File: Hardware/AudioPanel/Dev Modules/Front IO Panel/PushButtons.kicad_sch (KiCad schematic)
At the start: 38 parts, among them CN3 4x 10nF, CN4 4x 10nF, CN5 4x 10nF, U10 74HC14, U11 74HC14, U16 MCP23017_ML

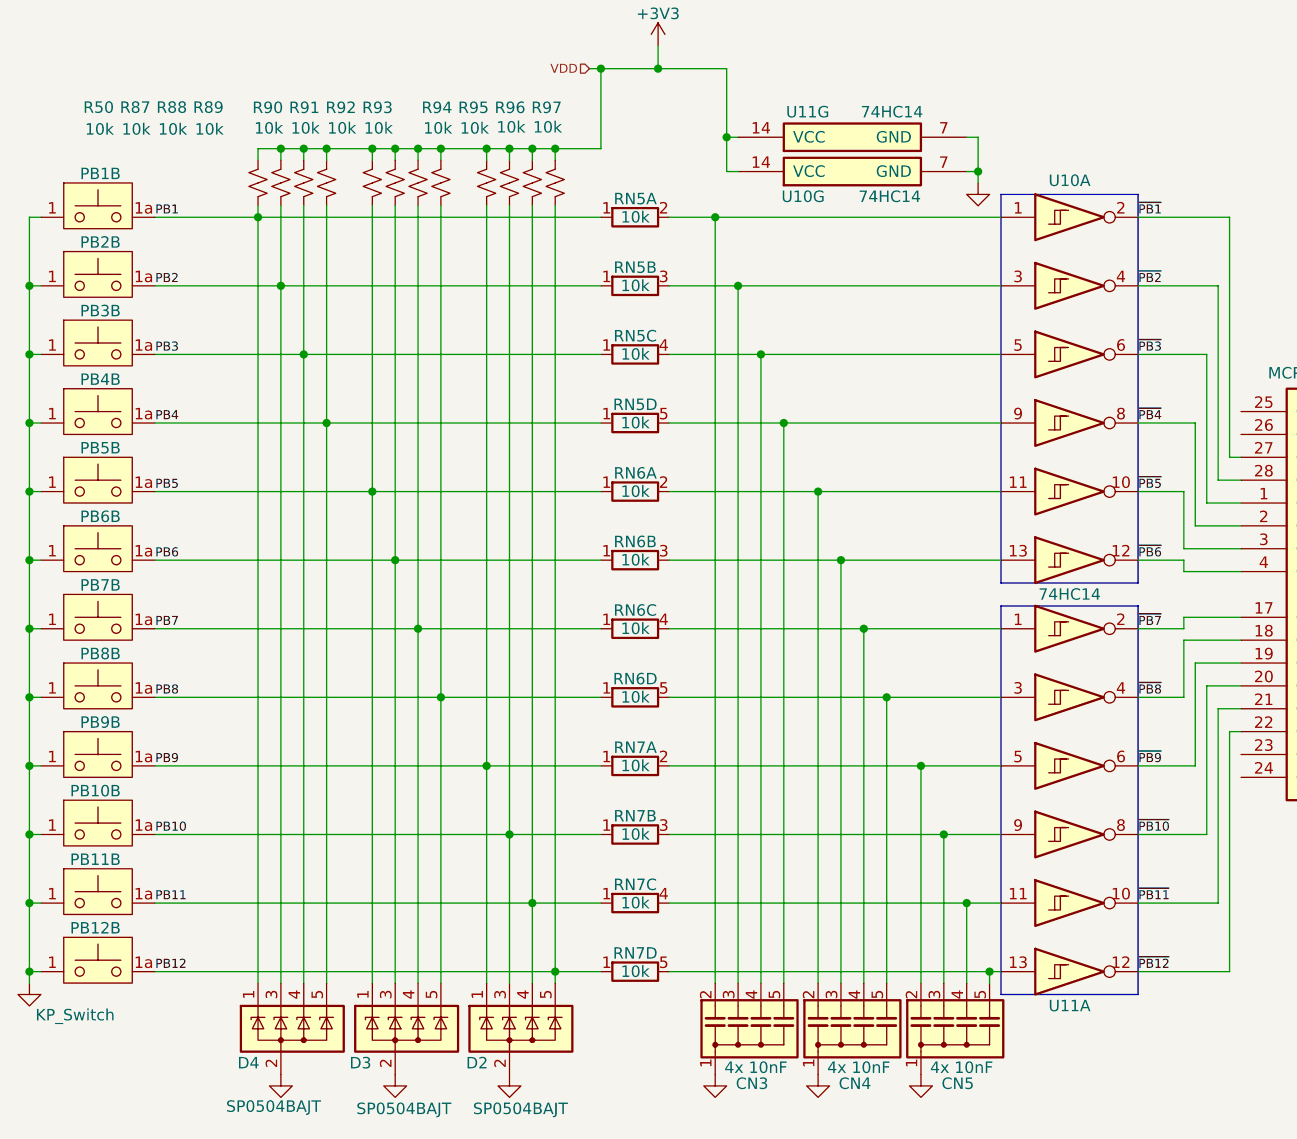
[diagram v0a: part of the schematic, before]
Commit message: Adding LEDs
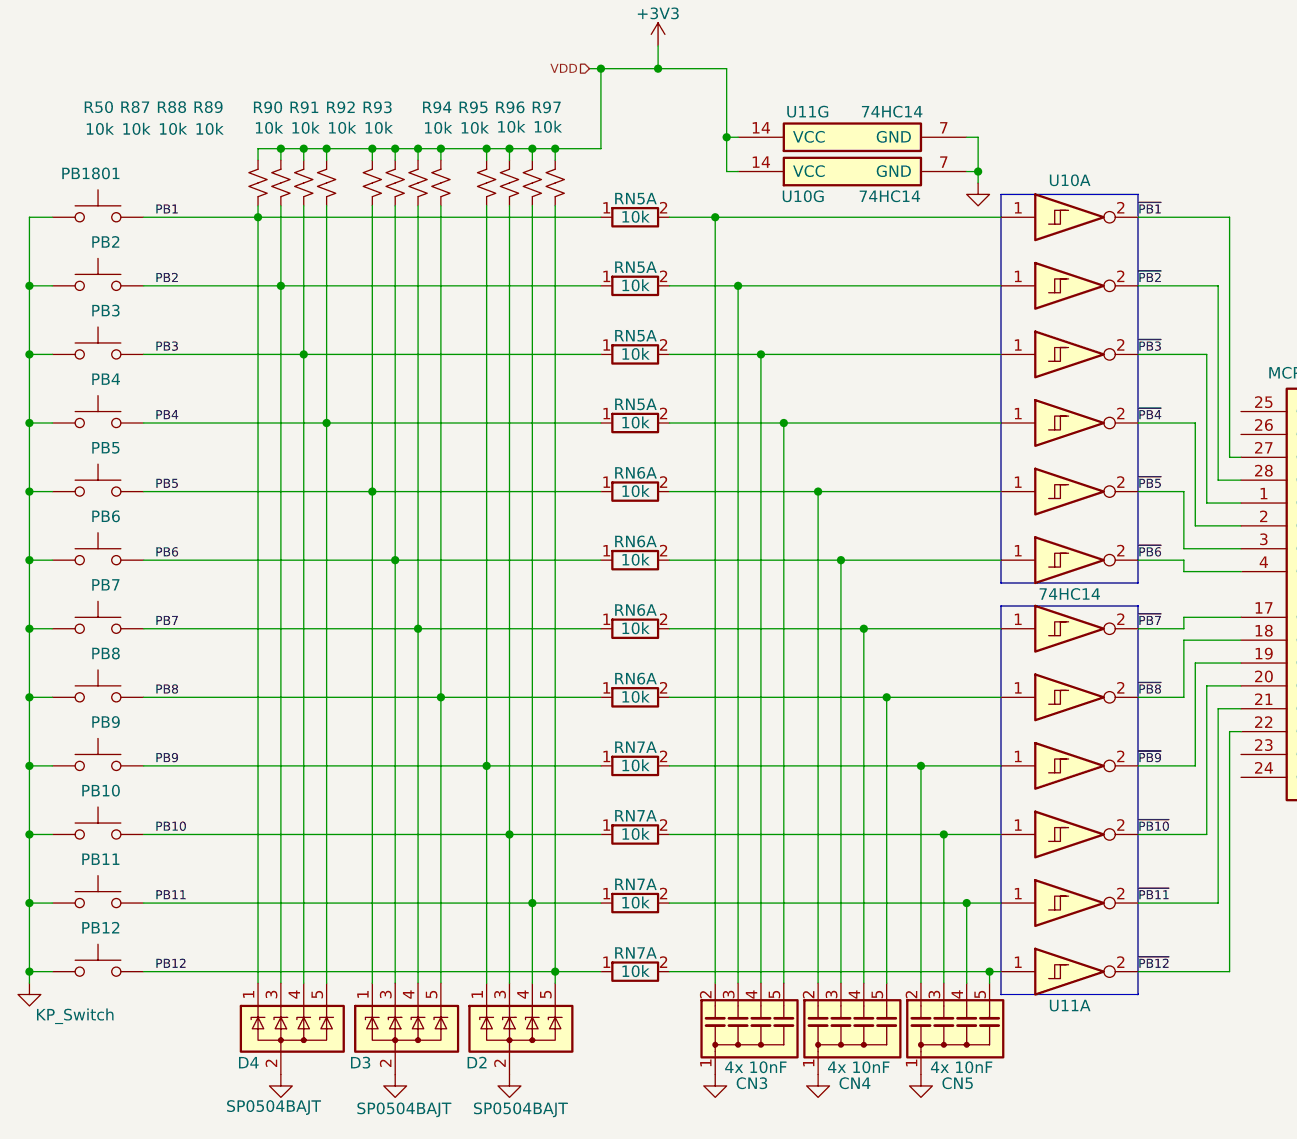
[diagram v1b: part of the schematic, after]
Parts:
- removed PB1: KP_Switch, symbol AudioPanelLibrary:KP_Switch
- added PB1801: KP_Switch, symbol Switch:SW_Push
- PB10, PB11, PB12, PB2, PB3, PB4, PB5, PB6, PB7, PB8, PB9: symbol AudioPanelLibrary:KP_Switch -> Switch:SW_Push
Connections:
- net GND: now also PB1801.1
- net PB1: now also PB1801.2
- net PB10: now also PB10.2; no longer PB10.1a (A)
- net PB11: now also PB11.2; no longer PB11.1a (A)
- net PB12: now also PB12.2; no longer PB12.1a (A)
- net PB2: now also PB2.2; no longer PB2.1a (A)
- net PB3: now also PB3.2; no longer PB3.1a (A)
- net PB4: now also PB4.2; no longer PB4.1a (A)
- net PB5: now also PB5.2; no longer PB5.1a (A)
- net PB6: now also PB6.2; no longer PB6.1a (A)
- net PB7: now also PB7.2; no longer PB7.1a (A)
- net PB8: now also PB8.2; no longer PB8.1a (A)
- net PB9: now also PB9.2; no longer PB9.1a (A)
- net ~{PB10}: now also U11.2; no longer U11.8
- net ~{PB11}: now also U11.2; no longer U11.10
- net ~{PB12}: now also U11.2; no longer U11.12
- net ~{PB2}: now also U10.2; no longer U10.4
- net ~{PB3}: now also U10.2; no longer U10.6
- net ~{PB4}: now also U10.2; no longer U10.8
- net ~{PB5}: now also U10.2; no longer U10.10
- net ~{PB6}: now also U10.2; no longer U10.12
- net ~{PB8}: now also U11.2; no longer U11.4
- net ~{PB9}: now also U11.2; no longer U11.6
- net at CN4.2 (C1), RN6.2 (R1.2): now also U10.1; no longer U10.11
- net at CN5.2 (C1), RN7.2 (R1.2): now also U11.1; no longer U11.5
- net at CN4.4 (C3), U11.1: now also RN6.2 (R1.2); no longer RN6.4 (R3.2)
- new net: CN5.3 (C2), RN7.2 (R1.2), U11.1
- new net: CN5.4 (C3), RN7.2 (R1.2), U11.1
- new net: CN5.5 (C4), RN7.2 (R1.2), U11.1
- new net: CN3.5 (C4), RN5.2 (R1.2), U10.1
- new net: CN3.4 (C3), RN5.2 (R1.2), U10.1
- new net: CN4.5 (C4), RN6.2 (R1.2), U11.1
- new net: CN3.3 (C2), RN5.2 (R1.2), U10.1
- new net: CN4.3 (C2), RN6.2 (R1.2), U10.1

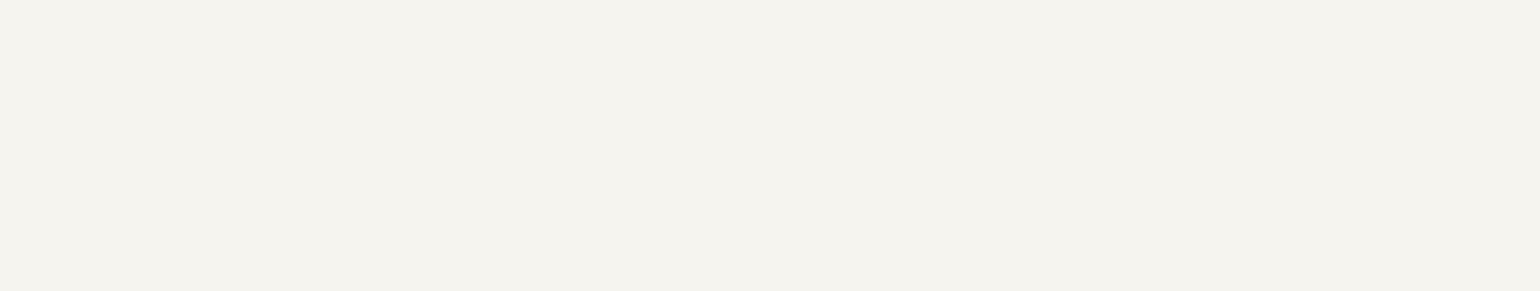
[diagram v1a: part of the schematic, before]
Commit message: Moved LEDs to pushbutton page
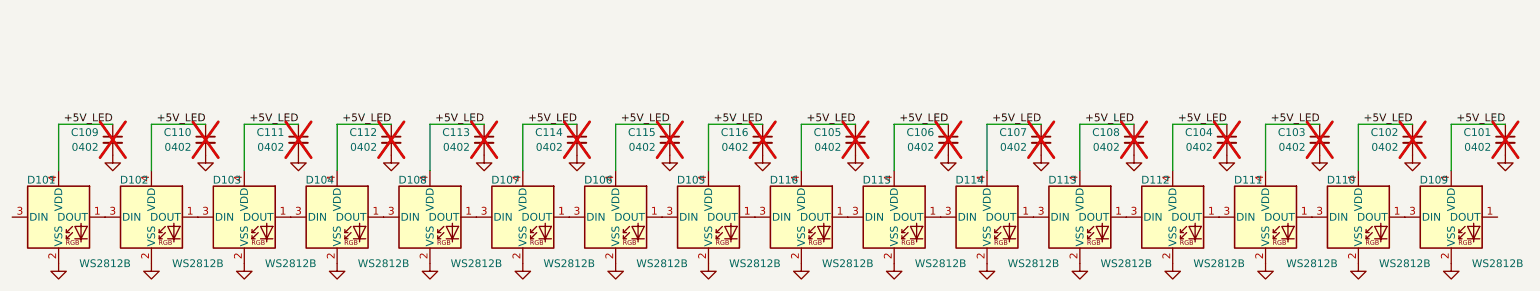
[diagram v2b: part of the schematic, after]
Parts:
- added C101, C102, C103, C104, C105, C106, C107, C108, C109, C110, C111, C112, C113, C114, C115, C116: 0402, Capacitor_SMD:C_0402_1005Metric, symbol Device:C_Small
- added D101, D102, D103, D104, D105, D106, D107, D108, D109, D110, D111, D112, D113, D114, D115, D116: WS2812B, Libraries:LED_WS2812B-2020_PLCC4_2.0x2.0mm, symbol LED:WS2812B-2020
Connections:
- net GND: now also C101.2, C102.2, C103.2, C104.2, C105.2, C106.2, C107.2, C108.2, C109.2, C110.2, C111.2, C112.2, C113.2, C114.2, C115.2, C116.2, D101.2 (VSS), D102.2 (VSS), D103.2 (VSS), D104.2 (VSS), D105.2 (VSS), D106.2 (VSS), D107.2 (VSS), D108.2 (VSS), D109.2 (VSS), D110.2 (VSS), D111.2 (VSS), D112.2 (VSS), D113.2 (VSS), D114.2 (VSS), D115.2 (VSS), D116.2 (VSS)
- new net: D104.1 (DOUT), D108.3 (DIN)
- new net: D103.1 (DOUT), D104.3 (DIN)
- new net: D107.3 (DIN), D108.1 (DOUT)
- new net: D109.3 (DIN), D110.1 (DOUT)
- new net: D115.3 (DIN), D116.1 (DOUT)
- new net: D105.1 (DOUT), D116.3 (DIN)
- new net: D113.3 (DIN), D114.1 (DOUT)
- new net: D114.3 (DIN), D115.1 (DOUT)
- new net: D106.3 (DIN), D107.1 (DOUT)
- new net: D110.3 (DIN), D111.1 (DOUT)
- new net: D111.3 (DIN), D112.1 (DOUT)
- new net: D101.1 (DOUT), D102.3 (DIN)
- new net: D105.3 (DIN), D106.1 (DOUT)
- new net: D102.1 (DOUT), D103.3 (DIN)
- new net: D112.3 (DIN), D113.1 (DOUT)
- new net +5V_LED: C101.1, C102.1, C103.1, C104.1, C105.1, C106.1, C107.1, C108.1, C109.1, C110.1, C111.1, C112.1, C113.1, C114.1, C115.1, C116.1, D101.4 (VDD), D102.4 (VDD), D103.4 (VDD), D104.4 (VDD), D105.4 (VDD), D106.4 (VDD), D107.4 (VDD), D108.4 (VDD), D109.4 (VDD), D110.4 (VDD), D111.4 (VDD), D112.4 (VDD), D113.4 (VDD), D114.4 (VDD), D115.4 (VDD), D116.4 (VDD)

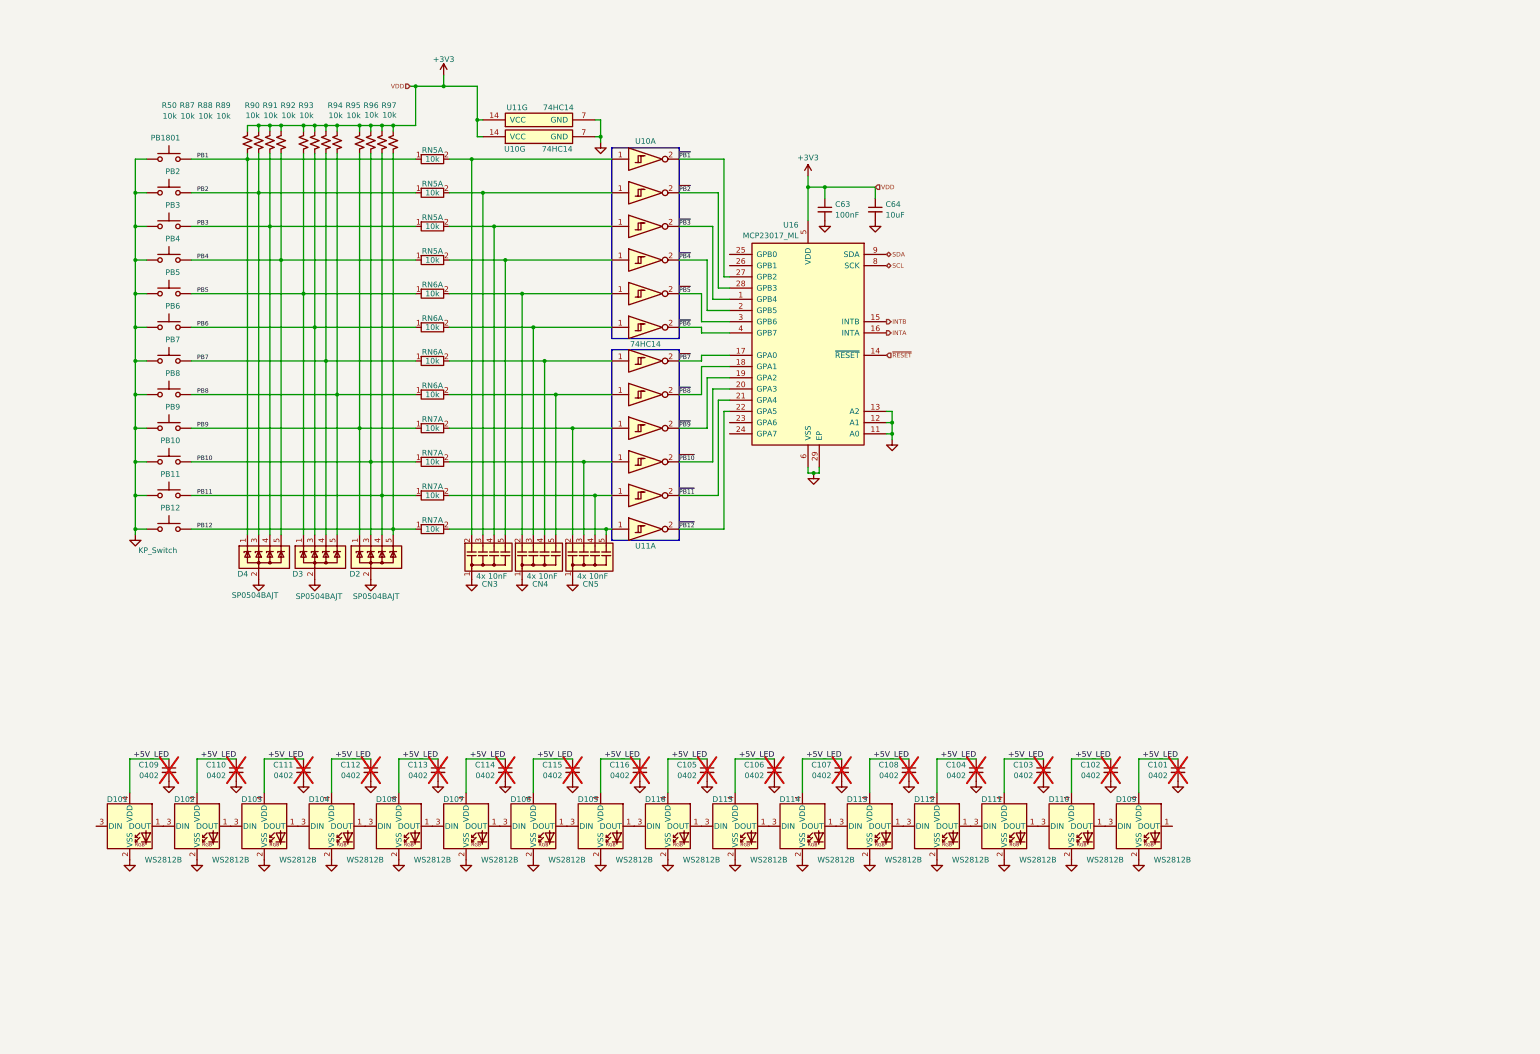
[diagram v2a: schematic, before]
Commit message: Added level shifters for all SAMD21s
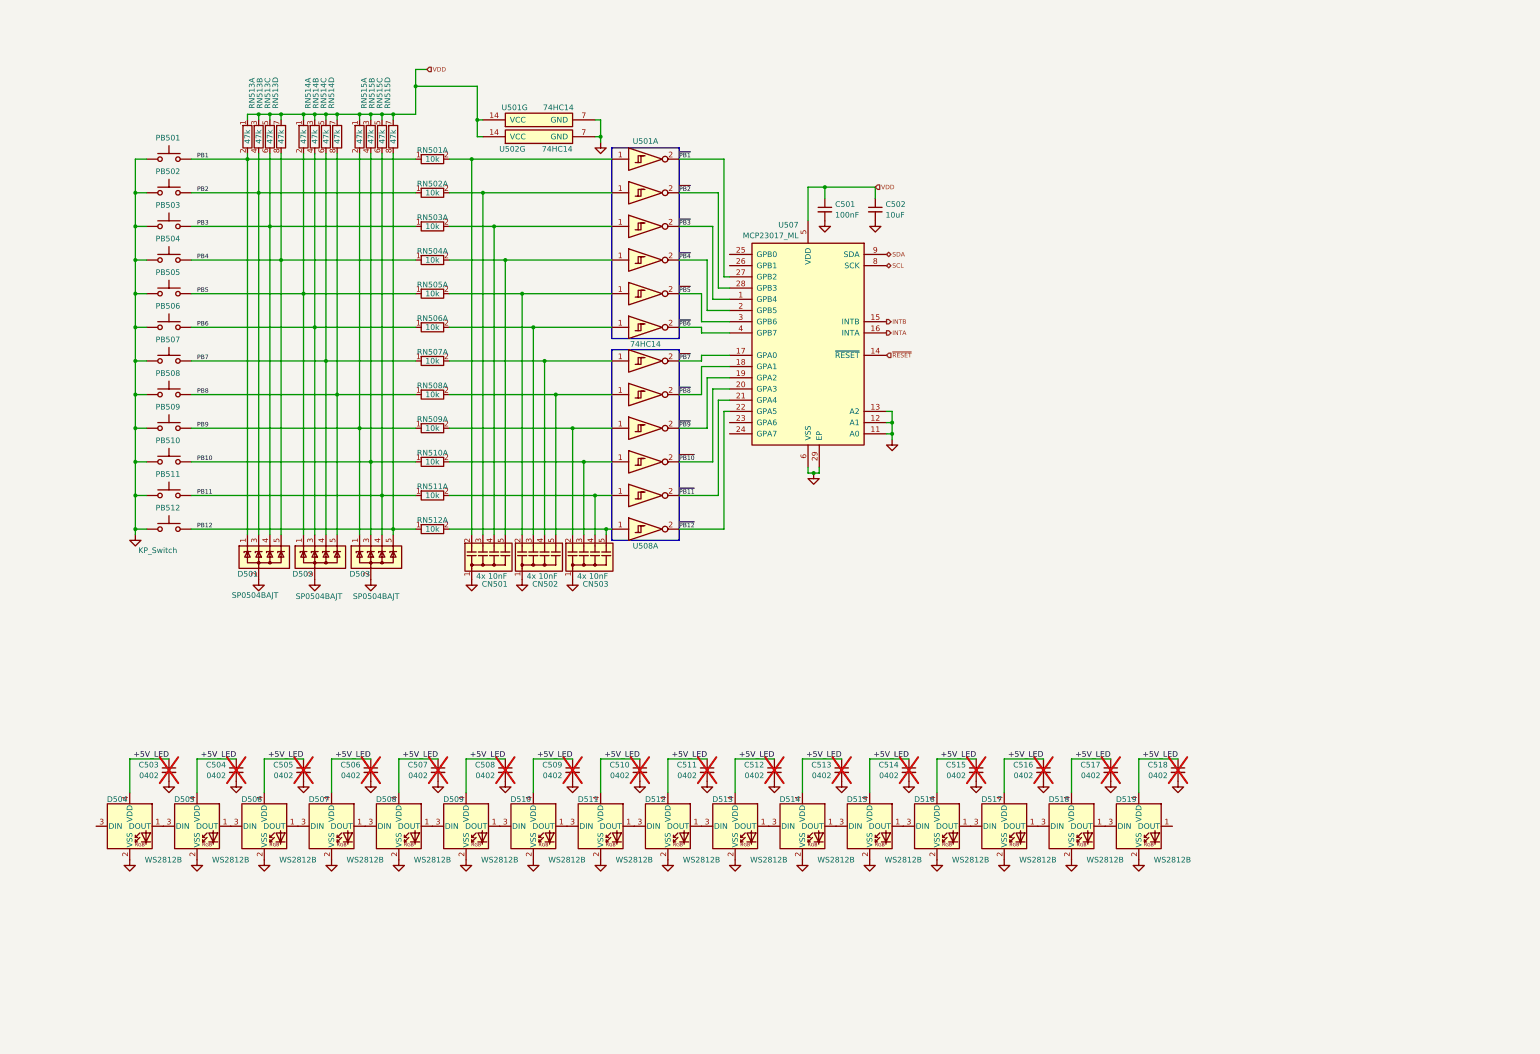
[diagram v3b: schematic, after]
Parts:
- removed R50, R87, R88, R89, R90, R91, R92, R93, R94, R95, R96, R97: 10k, symbol Device:R_Small_US
- added RN513, RN514, RN515: 47k, Resistor_SMD:R_Array_Convex_4x1206, symbol Library_MicSwitcher:R_Network04_Split
- renumbered C63 to C501, C64 to C502, C109 to C503, C110 to C504, C111 to C505, C112 to C506, C113 to C507, C114 to C508, C115 to C509, C116 to C510, C105 to C511, C106 to C512, C107 to C513, C108 to C514, C104 to C515, C103 to C516, C102 to C517, C101 to C518, CN3 to CN501, CN4 to CN502, CN5 to CN503, D4 to D501, D3 to D502, D2 to D503, D101 to D504, D102 to D505, D103 to D506, D104 to D507, D108 to D508, D107 to D509, D106 to D510, D105 to D511, D116 to D512, D115 to D513, D114 to D514, D113 to D515, D112 to D516, D111 to D517, D110 to D518, D109 to D519, PB1801 to PB501, PB2 to PB502, PB3 to PB503, PB4 to PB504, PB5 to PB505, PB6 to PB506, PB7 to PB507, PB8 to PB508, PB9 to PB509, PB10 to PB510, PB11 to PB511, PB12 to PB512, RN5 to RN501, RN5 to RN502, RN5 to RN503, RN5 to RN504, RN6 to RN505, RN6 to RN506, RN6 to RN507, RN6 to RN508, RN7 to RN509, RN7 to RN510, RN7 to RN511, RN7 to RN512, U11 to U501, U10 to U501, U10 to U502, U10 to U503, U10 to U504, U10 to U505, U10 to U506, U16 to U507, U11 to U508, U11 to U509, U11 to U510, U11 to U511, U11 to U512, U11 to U513
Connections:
- net PB1: now also RN513.2
- net PB10: now also RN515.4
- net PB11: now also RN515.6
- net PB12: now also RN515.8
- net PB2: now also RN513.4
- net PB3: now also RN513.6
- net PB4: now also RN513.8
- net PB5: now also RN514.2
- net PB6: now also RN514.4
- net PB7: now also RN514.6
- net PB8: now also RN514.8
- net PB9: now also RN515.2
- net +3V3 renamed VDD
- net VDD: now also RN513.1, RN513.3, RN513.5, RN513.7, RN514.1, RN514.3, RN514.5, RN514.7, RN515.1, RN515.3, RN515.5, RN515.7
